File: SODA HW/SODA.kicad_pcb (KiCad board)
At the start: 2 copper layers, 39 x 20 mm, 37 parts, among them CON1 USB-MICRO-B, P1 CONN_02X05, P2 CONN_01X01, P3 CONN_01X01, P4 CONN_01X01, P5 CONN_01X01, P6 CONN_01X01, SW1 SW_PUSH, U1 TC1014-3.3V, U2 12Mhz_SMD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

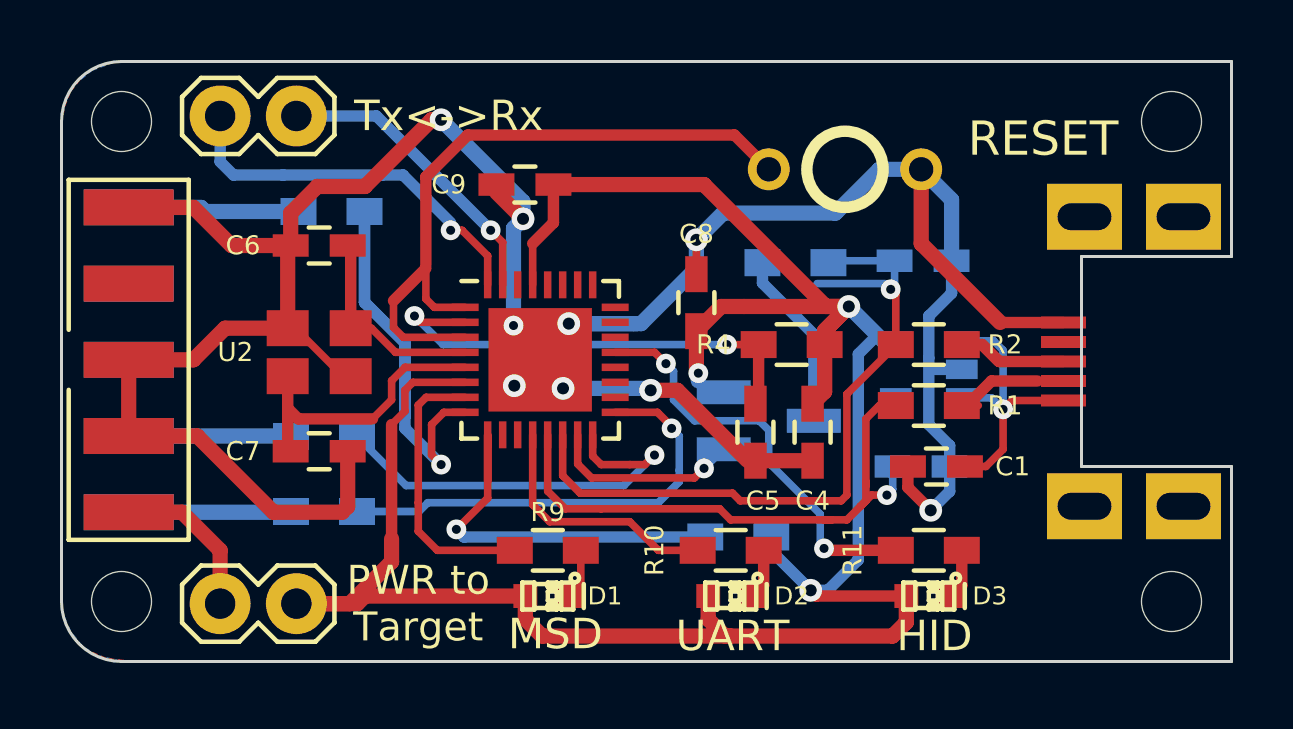
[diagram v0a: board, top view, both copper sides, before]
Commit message: Board name modified and gerber file generated
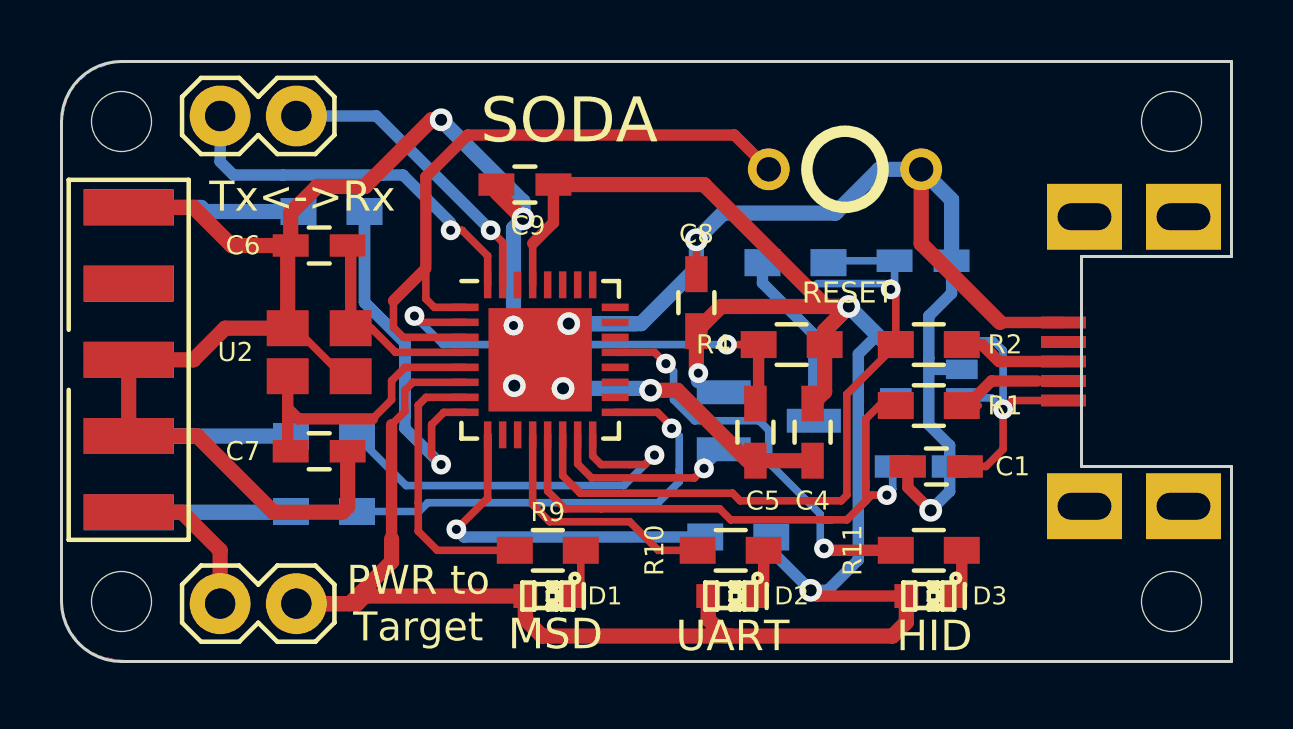
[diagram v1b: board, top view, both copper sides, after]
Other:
- board text added: "SODA"
- board text added: "v1.0"
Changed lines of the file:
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@@
-(kicad_pcb (version 4) (host pcbnew "(2015-01-16 BZR 5376)-product")
+(kicad_pcb (version 4) (host pcbnew 4.0.4-stable)
   (general
     (links 68)
     (no_connects 0)
-    (area 139.949999 49.949999 179.050001 70.050001)
+    (area 137.228867 44.328675 191.212953 77.427868)
     (thickness 1.6)
-    (drawings 17)
+    (drawings 21)
     (tracks 357)
     (zones 0)
@@
     (visible_elements 7FFFFF7F)
     (pcbplotparams
-      (layerselection 0x00030_80000001)
+      (layerselection 0x000f0_80000001)
       (usegerberextensions false)
-      (excludeedgelayer true)
+      (excludeedgelayer false)
       (linewidth 0.100000)
       (plotframeref false)
@@
       (outputformat 1)
       (mirror false)
-      (drillshape 1)
+      (drillshape 0)
       (scaleselection 1)
-      (outputdirectory ""))
+      (outputdirectory "Gerber file v1.0/"))
   )
   (net 0 "")
@@
     (tags "capacitor 0603")
     (attr smd)
-    (fp_text reference C9 (at -2.54 0) (layer F.SilkS)
+    (fp_text reference C9 (at 0.1016 1.3716) (layer F.SilkS)
       (effects (font (size 0.635 0.635) (thickness 0.15)))
     )
@@
       (xy 7 -5.15)) (layer B.SilkS) (width 0.01))
   )
-  (gr_text Tx<->Rx (at 152.908 51.816) (layer F.SilkS)
-    (effects (font (size 1.016 1.016) (thickness 0.254)))
+  (dimension 39.015591 (width 0.3) (layer Margin)
+    (gr_text "39.016 mm" (at 159.578514 75.925508 0.4476141709) (layer Margin)
+      (effects (font (size 1.5 1.5) (thickness 0.3)))
+    )
+    (feature1 (pts (xy 179.0192 67.2592) (xy 179.096261 77.123067)))
+    (feature2 (pts (xy 140.0048 67.564) (xy 140.081861 77.427867)))
+    (crossbar (pts (xy 140.060768 74.727949) (xy 179.075168 74.423149)))
+    (arrow1a (pts (xy 179.075168 74.423149) (xy 177.95328 75.018352)))
+    (arrow1b (pts (xy 179.075168 74.423149) (xy 177.944117 73.845547)))
+    (arrow2a (pts (xy 140.060768 74.727949) (xy 141.191819 75.305551)))
+    (arrow2b (pts (xy 140.060768 74.727949) (xy 141.182656 74.132746)))
+  )
+  (dimension 20.015264 (width 0.3) (layer Margin)
+    (gr_text "20.015 mm" (at 184.712953 59.980284 270.1454204) (layer Margin)
+      (effects (font (size 1.5 1.5) (thickness 0.3)))
+    )
+    (feature1 (pts (xy 179.0192 70.0024) (xy 186.088349 69.984458)))
+    (feature2 (pts (xy 178.9684 49.9872) (xy 186.037549 49.969258)))
+    (crossbar (pts (xy 183.337558 49.976111) (xy 183.388358 69.991311)))
+    (arrow1a (pts (xy 183.388358 69.991311) (xy 182.79908 68.866299)))
+    (arrow1b (pts (xy 183.388358 69.991311) (xy 183.971918 68.863322)))
+    (arrow2a (pts (xy 183.337558 49.976111) (xy 182.753998 51.1041)))
+    (arrow2b (pts (xy 183.337558 49.976111) (xy 183.926836 51.101123)))
+  )
+  (gr_text v1.0 (at 172.9232 68.1736) (layer B.SilkS)
+    (effects (font (size 1 1) (thickness 0.25)) (justify mirror))
+  )
+  (gr_text SODA (at 156.9212 51.9684) (layer F.SilkS)
+    (effects (font (size 1.5 1.5) (thickness 0.3)))
+  )
+  (gr_text Tx<->Rx (at 148.0312 54.5084) (layer F.SilkS)
+    (effects (font (size 1 1) (thickness 0.25)))
   )
   (gr_text "PWR to\nTarget" (at 151.892 68.072) (layer F.SilkS)
@@
   (gr_arc (start 142 68) (end 142 70) (angle 90) (layer Edge.Cuts) (width 0.1))
   (gr_arc (start 142 52) (end 140 52) (angle 90) (layer Edge.Cuts) (width 0.1))
-  (gr_text RESET (at 172.72 52.578) (layer F.SilkS)
-    (effects (font (size 1.143 1.143) (thickness 0.28575)))
+  (gr_text RESET (at 166.2176 57.7088) (layer F.SilkS)
+    (effects (font (size 0.7 0.7) (thickness 0.125)))
   )
   (gr_text HID (at 169.1005 69.1515) (layer F.SilkS)
